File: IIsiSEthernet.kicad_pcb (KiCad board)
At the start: 4 copper layers, 124 x 38 mm, 56 parts, among them IC1 SST39SF010A-70-4C-WHE, J1 650906-5, J3 USB_B_Micro, J5 RJ45_Amphenol_RJMG1BD3B8K1ANR, J7 AVR-JTAG-10, U2 ATF1502ASL-25AU44, U3 ENC624J600-I_PT, U4 LD1117S33TR_SOT223, X2 ASE-xxxMHz

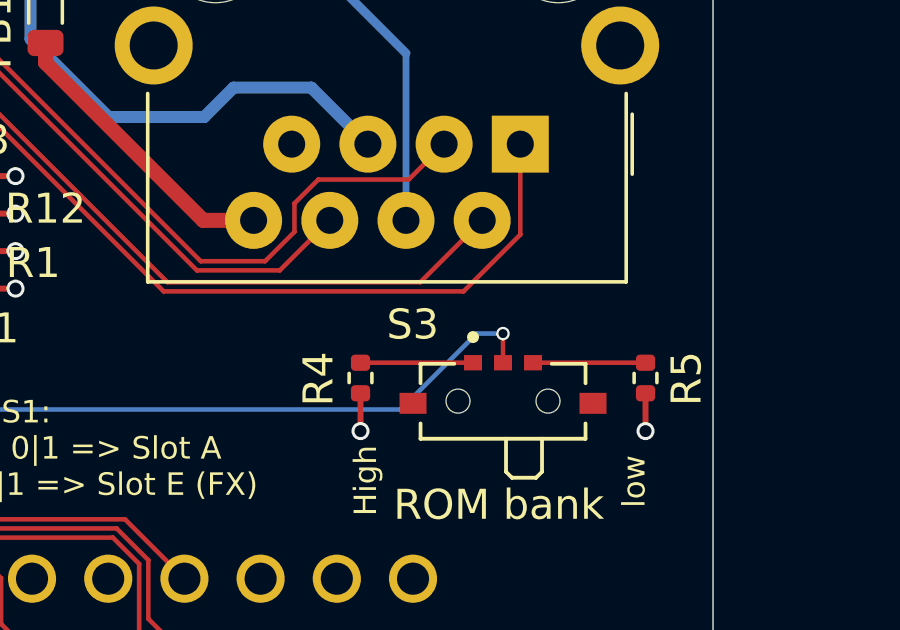
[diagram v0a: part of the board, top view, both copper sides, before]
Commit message: 27->33 ohms (basic...)
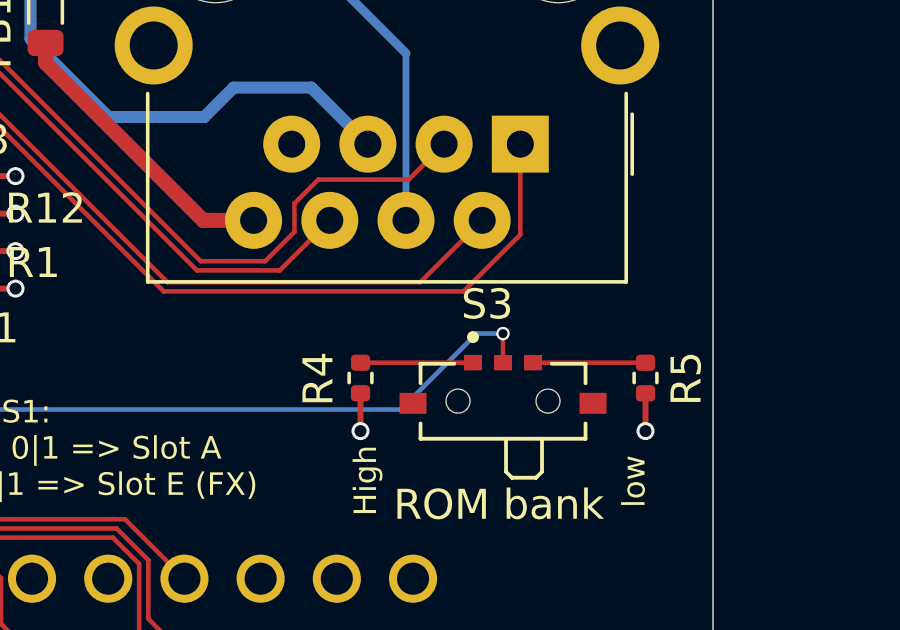
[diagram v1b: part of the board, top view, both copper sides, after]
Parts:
- R6: value 27 -> 33
